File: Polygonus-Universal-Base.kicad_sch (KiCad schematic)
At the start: 9 parts, among them J4 Polygonus_Plugs, U1 f042_wideband_module, U14 f042_wideband_module

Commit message: Fixed WBO pin allocation
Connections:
- net 12V_KEY: now also Motronic_88pin1.44; no longer Motronic_88pin1.21
- net 12V_MR_FUSE: now also Motronic_88pin1.67; no longer Motronic_88pin1.10, Motronic_88pin1.37
- net GND: now also Motronic_88pin1.17, Motronic_88pin1.18, Motronic_88pin1.45, Motronic_88pin1.46; no longer Motronic_88pin1.36, Motronic_88pin1.44, Motronic_88pin1.67, Motronic_88pin1.8, Motronic_88pin1.9
- net HeaterNeg: now also Motronic_88pin1.21
- net HeaterNeg2: now also Motronic_88pin1.35
- net KNOCK_1: now also Motronic_88pin1.8; no longer Motronic_88pin1.35
- net LSU_Ip2: now also Motronic_88pin1.10; no longer Motronic_88pin1.46
- net LSU_Rtrim2: now also Motronic_88pin1.9; no longer Motronic_88pin1.45
- net LSU_Un2: now also Motronic_88pin1.36; no longer Motronic_88pin1.17
- net LSU_Vm2: now also Motronic_88pin1.37; no longer Motronic_88pin1.18

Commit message: Added DRV8825 footprint
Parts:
- added A1: Pololu_Breakout_DRV8825, Module:Pololu_Breakout-16_15.2x20.3mm, symbol Driver_Motor:Pololu_Breakout_DRV8825
- added JP1 (x4): Jumper_3_Open, Jumper:SolderJumper-3_P2.0mm_Open_TrianglePad1.0x1.5mm, symbol Jumper:Jumper_3_Open
- added R17, R18: 1k, Resistor_SMD:R_0805_2012Metric, symbol hellen-one-common:Res
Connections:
- net +5V: now also A1.13 (~{RST}), A1.14 (~{SLP}), R17.1, R18.2
- net 12V_MR_FUSE: now also A1.8 (VMOT)
- net GND: now also A1.1 (GND), A1.10 (M0), A1.11 (M1), A1.12 (M2), A1.7 (GND), A1.9 (~{EN})
- net HS1: now also JP1.2 (C); no longer J4.68 (Pin_68)
- net HS2: now also JP1.2 (C); no longer J4.67 (Pin_67)
- net HS3: now also JP1.2 (C); no longer J4.66 (Pin_66)
- net HS4: now also JP1.2 (C); no longer J4.65 (Pin_65)
- net LS10ADD: now also A1.16 (DIR), R17.2
- net LS9ADD: now also A1.15 (STEP), R18.1
- new net: A1.6 (B2), JP1.1 (A)
- new net: A1.5 (B1), JP1.1 (A)
- new net: A1.4 (A1), JP1.1 (A)
- new net: A1.3 (A2), JP1.1 (A)
- new net HS1_IN: J4.68 (Pin_68), JP1.3 (B)
- new net HS2_IN: J4.67 (Pin_67), JP1.3 (B)
- new net HS3_IN: J4.66 (Pin_66), JP1.3 (B)
- new net HS4_IN: J4.65 (Pin_65), JP1.3 (B)

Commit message: default set HS
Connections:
- net HS1_IN is gone; now on net HS1: J4.68 (Pin_68), JP1.3 (B)
- net HS2_IN is gone; now on net HS2: J4.67 (Pin_67), JP1.3 (B)
- net HS3_IN is gone; now on net HS3: J4.66 (Pin_66), JP1.3 (B)
- net HS4_IN is gone; now on net HS4: J4.65 (Pin_65), JP1.3 (B)
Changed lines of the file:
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@@
     (effects (font (size 1.27 1.27)) (justify right bottom))
   )
-  (label "HS2_IN" (at 73.66 248.92 0) (fields_autoplaced)
+  (label "HS2" (at 73.66 248.92 0) (fields_autoplaced)
     (effects (font (size 1.27 1.27)) (justify left bottom))
   )
@@
     (effects (font (size 1.27 1.27)) (justify left bottom))
   )
-  (label "HS3_IN" (at 219.71 86.36 180) (fields_autoplaced)
+  (label "HS3" (at 219.71 86.36 180) (fields_autoplaced)
     (effects (font (size 1.27 1.27)) (justify right bottom))
   )
@@
     (effects (font (size 1.27 1.27)) (justify right bottom))
   )
-  (label "HS3_IN" (at 73.66 226.06 0) (fields_autoplaced)
+  (label "HS3" (at 73.66 226.06 0) (fields_autoplaced)
     (effects (font (size 1.27 1.27)) (justify left bottom))
   )
@@
     (effects (font (size 1.27 1.27)) (justify right bottom))
   )
-  (label "HS1_IN" (at 219.71 91.44 180) (fields_autoplaced)
+  (label "HS1" (at 219.71 91.44 180) (fields_autoplaced)
     (effects (font (size 1.27 1.27)) (justify right bottom))
   )
@@
     (effects (font (size 1.27 1.27)) (justify right bottom))
   )
-  (label "HS4_IN" (at 219.71 83.82 180) (fields_autoplaced)
+  (label "HS4" (at 219.71 83.82 180) (fields_autoplaced)
     (effects (font (size 1.27 1.27)) (justify right bottom))
   )
@@
     (effects (font (size 1.27 1.27)) (justify right bottom))
   )
-  (label "HS1_IN" (at 73.66 260.35 0) (fields_autoplaced)
+  (label "HS1" (at 73.66 260.35 0) (fields_autoplaced)
     (effects (font (size 1.27 1.27)) (justify left bottom))
   )
@@
     (effects (font (size 1.27 1.27)) (justify right bottom))
   )
-  (label "HS2_IN" (at 219.71 88.9 180) (fields_autoplaced)
+  (label "HS2" (at 219.71 88.9 180) (fields_autoplaced)
     (effects (font (size 1.27 1.27)) (justify right bottom))
   )
@@
     (effects (font (size 1.27 1.27)) (justify right bottom))
   )
-  (label "HS4_IN" (at 73.66 237.49 0) (fields_autoplaced)
-    (effects (font (size 1.27 1.27)) (justify left bottom))
-  )
+  (label "HS4" (at 73.66 237.49 0) (fields_autoplaced)
+    (effects (font (size 1.27 1.27)) (justify left bottom))
+  )

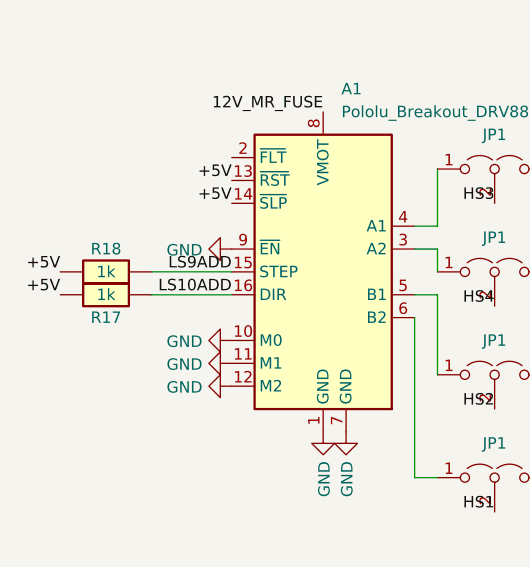
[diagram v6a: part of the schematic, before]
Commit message: stepper ls direct to logic pins
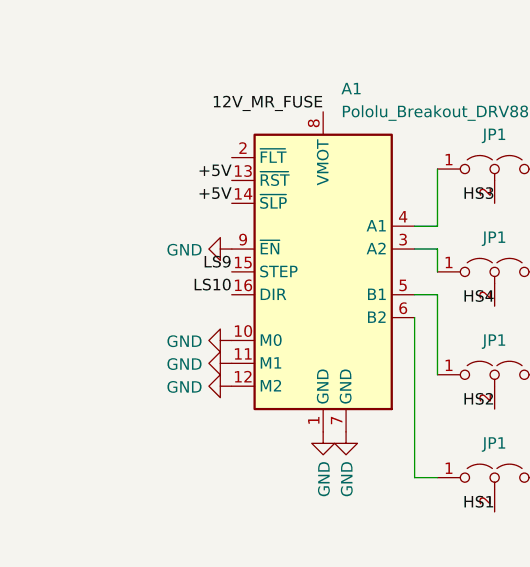
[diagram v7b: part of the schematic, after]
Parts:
- removed R17, R18: 1k, Resistor_SMD:R_0805_2012Metric, symbol hellen-one-common:Res
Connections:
- net LS10: now also A1.16 (DIR)
- net LS10ADD: no longer A1.16 (DIR)
- net LS9: now also A1.15 (STEP)
- net LS9ADD: no longer A1.15 (STEP)
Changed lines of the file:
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@@
-    (stroke (width 0) (type default))
-  )
-  (wire (pts (xy 29.21 240.03) (xy 38.1 240.03))
     (stroke (width 0) (type default))
   )
@@
   )
   (wire (pts (xy 279.4 66.04) (xy 271.78 66.04))
-    (stroke (width 0) (type default))
-  )
-  (wire (pts (xy 29.21 237.49) (xy 38.1 237.49))
     (stroke (width 0) (type default))
   )
@@
     (effects (font (size 1.27 1.27)) (justify right bottom))
   )
-  (label "LS10ADD" (at 38.1 240.03 180) (fields_autoplaced)
+  (label "LS10" (at 38.1 240.03 180) (fields_autoplaced)
     (effects (font (size 1.27 1.27)) (justify right bottom))
   )
@@
     (effects (font (size 1.27 1.27)) (justify right bottom))
   )
-  (label "LS9ADD" (at 38.1 237.49 180) (fields_autoplaced)
+  (label "LS9" (at 38.1 237.49 180) (fields_autoplaced)
     (effects (font (size 1.27 1.27)) (justify right bottom))
   )
@@
     (effects (font (size 1.27 1.27)) (justify right bottom))
   )
-  (label "+5V" (at 19.05 237.49 180) (fields_autoplaced)
-    (effects (font (size 1.27 1.27)) (justify right bottom))
-  )
   (label "AV9" (at 168.91 138.43 180) (fields_autoplaced)
     (effects (font (size 1.27 1.27)) (justify right bottom))
@@
   )
   (label "ExtraLSD" (at 271.78 110.49 180) (fields_autoplaced)
-    (effects (font (size 1.27 1.27)) (justify right bottom))
-  )
-  (label "+5V" (at 19.05 240.03 180) (fields_autoplaced)
     (effects (font (size 1.27 1.27)) (justify right bottom))
   )
@@
     )
   )
-  (symbol (lib_id "hellen-one-common:Res") (at 29.21 237.49 0) (mirror y) (unit 1)
-    (in_bom yes) (on_board yes) (dnp no)
-    (property "Reference" "R18" (at 24.13 234.95 0)
-      (effects (font (size 1.27 1.27)))
-    )
-    (property "Value" "1k" (at 24.13 237.49 0)
-      (effects (font (size 1.27 1.27)))
-    )
-    (property "Footprint" "Resistor_SMD:R_0805_2012Metric" (at 25.4 241.3 0)
-      (effects (font (size 1.27 1.27)) hide)
-    )
-    (property "Datasheet" "" (at 29.21 237.49 0)
-      (effects (font (size 1.27 1.27)) hide)
-    )
-    (property "LCSC" "C21190" (at 29.21 237.49 0)
-      (effects (font (size 1.27 1.27)) hide)
-    )
-    (pin "1")
-    (pin "2")
-    (instances
-      (project "Polygonus-Universal-Base"
-        (path "/e63e39d7-6ac0-4ffd-8aa3-1841a4541b55"
-          (reference "R18") (unit 1)
-        )
-      )
-    )
-  )
   (symbol (lib_id "Jumper:Jumper_3_Open") (at 67.31 248.92 0) (unit 1)
     (in_bom yes) (on_board yes) (dnp no)
@@
         )
       )
-    )
-  )
-  (symbol (lib_id "hellen-one-common:Res") (at 19.05 240.03 0) (mirror x) (unit 1)
-    (in_bom yes) (on_board yes) (dnp no)
-    (property "Reference" "R17" (at 24.13 242.57 0)
-      (effects (font (size 1.27 1.27)))
-    )
-    (property "Value" "1k" (at 24.13 240.03 0)
-      (effects (font (size 1.27 1.27)))
-    )
-    (property "Footprint" "Resistor_SMD:R_0805_2012Metric" (at 22.86 236.22 0)
-      (effects (font (size 1.27 1.27)) hide)
-    )
-    (property "Datasheet" "" (at 19.05 240.03 0)
-      (effects (font (size 1.27 1.27)) hide)
-    )
-    (property "LCSC" "C21190" (at 19.05 240.03 0)
-      (effects (font (size 1.27 1.27)) hide)
-    )
-    (pin "1")
-    (pin "2")
-    (instances
-      (project "Polygonus-Universal-Base"
-        (path "/e63e39d7-6ac0-4ffd-8aa3-1841a4541b55"
-          (reference "R17") (unit 1)
-        )
-      )

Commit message: production files v1.0
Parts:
- C10: footprint Resistor_SMD:R_0805_2012Metric -> Capacitor_SMD:C_0805_2012Metric
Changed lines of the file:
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@@
       (effects (font (size 1.27 1.27)))
     )
-    (property "Footprint" "Resistor_SMD:R_0805_2012Metric" (at 223.52 196.85 0)
+    (property "Footprint" "Capacitor_SMD:C_0805_2012Metric" (at 223.52 196.85 0)
       (effects (font (size 1.27 1.27)) hide)
     )
